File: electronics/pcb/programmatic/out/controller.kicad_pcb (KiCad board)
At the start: 2 copper layers, 140 x 100 mm, 60 parts, among them Q1 Q1, Q2 Q2

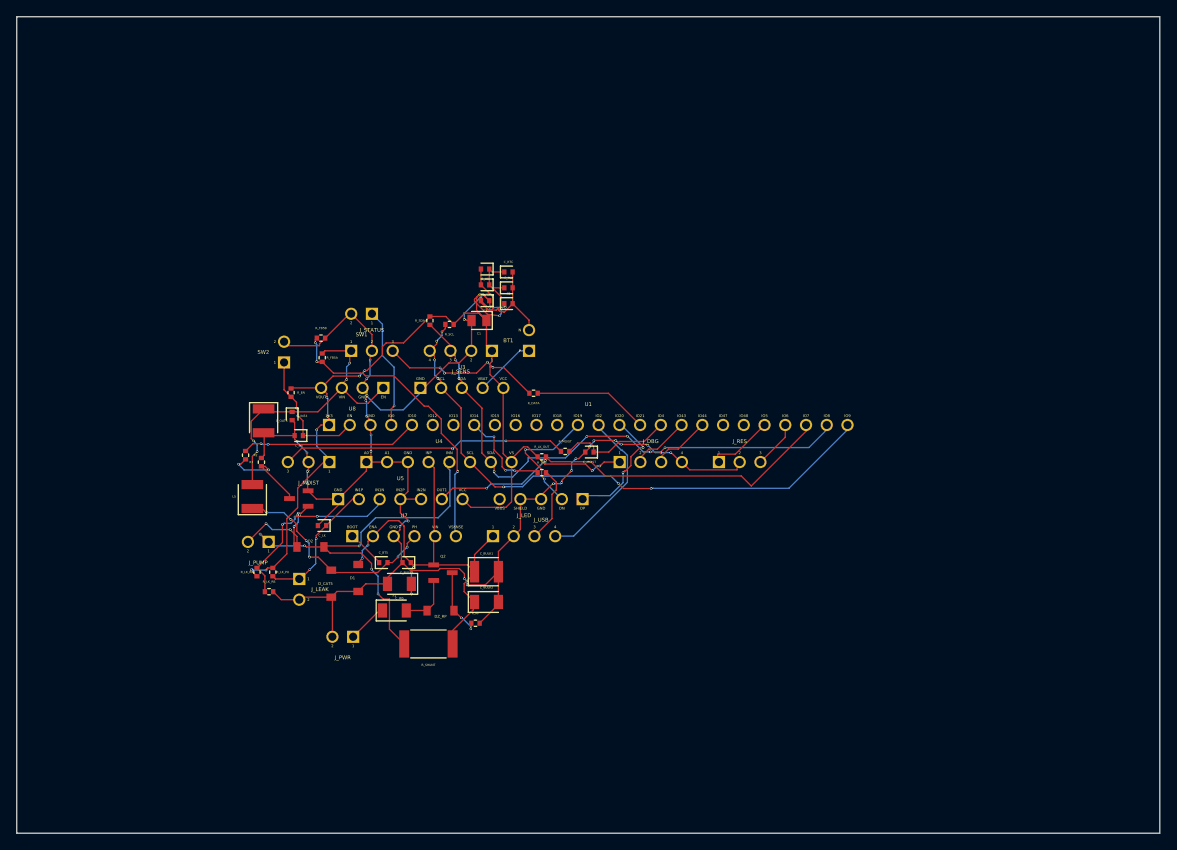
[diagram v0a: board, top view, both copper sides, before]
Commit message: electronics+docs: rendered electronics-design doc; retire KiCad (tscircuit is the PCB tool)
Adds a published, render-rich electronics design doc and makes the PCB toolchain
coherent by retiring the unused KiCad path.

docs/electronics-design.md (new): an extensive, reviewable walkthrough of the
controller board — a per-subsystem tour (power input/protection, DC-DC rails,
MCU+USB/UART, I2C+RTC+current monitor, moisture/reservoir, leak detect, the
fail-OFF pump drive, LED dim+status), the safety design, the connector handoff,
the BOM, and the headless netlist->Gerbers flow. 10 renders in
docs/assets/renders/ (e-*.png), generated from the netlist:
  * 8 per-subsystem schematics (clean, labelled — the "each part" views)
  * full-board 3D + top-copper (the auto-routed draft, labelled as such)
Render pipeline: gen_tscircuit.py now emits per-subsystem blocks (blocks/);
render.sh produces all PNGs via tscircuit + resvg. Indexed in docs/README.md.

KiCad retired (ECO-002): the board is designed with the headless tscircuit flow
(electronics/pcb/programmatic/), which we can actually run; KiCad needed a GUI we
don't use. Removed pcb/kicad/, the empty pcb/gerbers/ and pcb/ibom/ placeholders,
and the eda kicad-cli CI job (it only ever skipped). Reframed the netlist/fab/
design-rule docs and the WI-EE-03/04/07/09 statuses to the tscircuit flow. The
netlist still emits controller.net and the flow exports controller.kicad_pcb, so
KiCad remains available as optional interchange — the bridge is kept, the tool is
not required. The committed electrical gate (netlist ERC in the BOM job) is
unchanged. All checks green; bom_check --strict still passes.

Co-Authored-By: Claude Opus 4.8 (1M context) <noreply@anthropic.com>
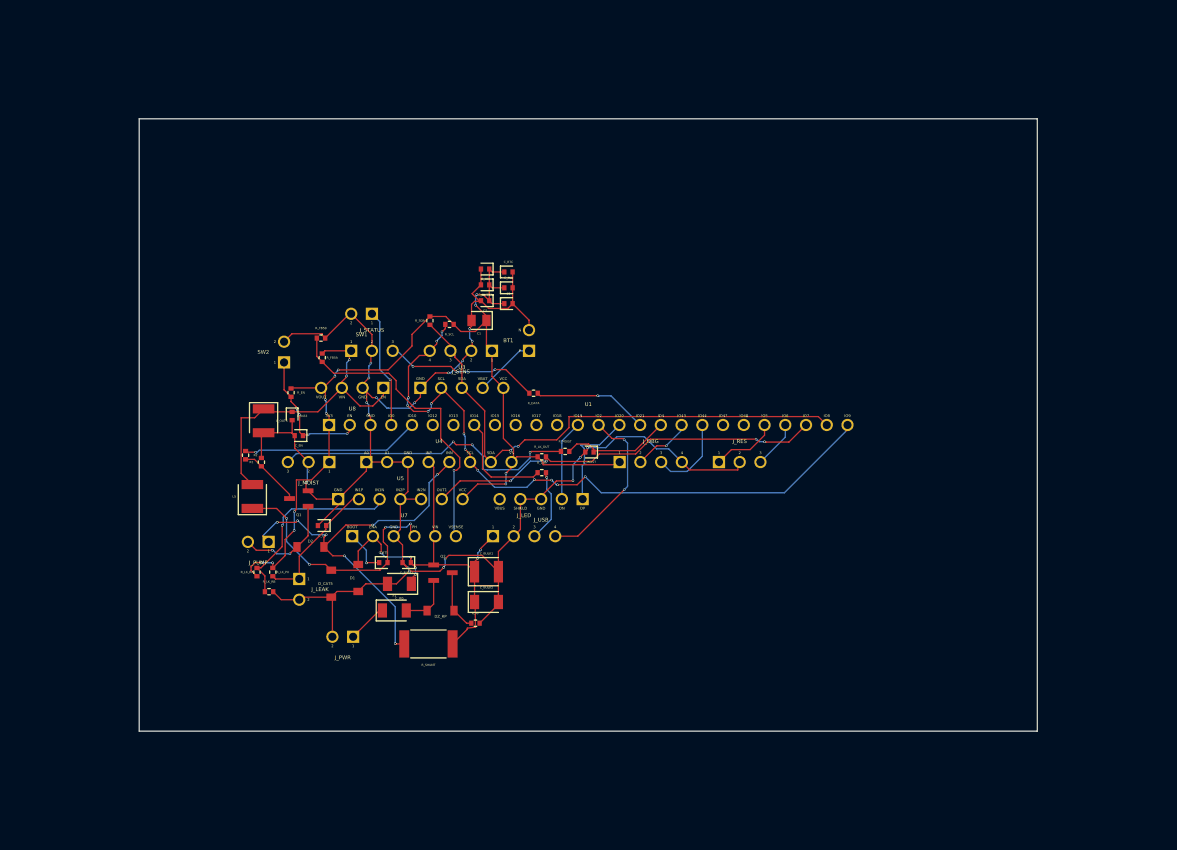
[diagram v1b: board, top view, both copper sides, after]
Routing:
- net P3V3: track 133.5 -> 118.9 mm, vias 13 -> 12
- net SCL: track 71.9 -> 82.4 mm, vias 7 -> 13
- net USB_DM: track 15.6 -> 9.89 mm, vias 2 -> 0
- net P24V: track 56.8 -> 51.4 mm, vias 4 -> 6
- net PH5: track 26.7 -> 31.4 mm, vias 6 -> 4
- net GND: track 220.4 -> 216.1 mm, vias 27 -> 18
- net PUMP_GATE: track 11.6 -> 7.67 mm, vias 2 -> 0
- net MOIST_SIG: track 35.1 -> 38.3 mm, vias 2 -> 3
- net USB_DP: track 15.5 -> 12.7 mm, vias 2 -> 0
- net UART_RX: track 7.32 -> 10.1 mm
- net SDA: track 67.2 -> 64.6 mm, vias 7 -> 2
- net PUMP_RET: track 15.0 -> 12.5 mm, vias 4 -> 2
- net LEAK_DET: track 52.0 -> 49.6 mm, vias 2 -> 4
- net P5V: track 36.7 -> 39.1 mm, vias 4 -> 2
- net FB5: track 36.6 -> 38.5 mm, vias 3 -> 1
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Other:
- board size 140 x 100 mm -> 110 x 75 mm
